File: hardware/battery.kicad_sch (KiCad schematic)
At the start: 40 parts, among them J301 B2B-XH-A, J302 PRPC001DAAN-RC, Q301 DMG2305UX-7, Q302 DMN2005, Q303 DMN2005, U301 BQ29728DSER, U302 MCP73833T-FCI/MF, U303 MAX17048

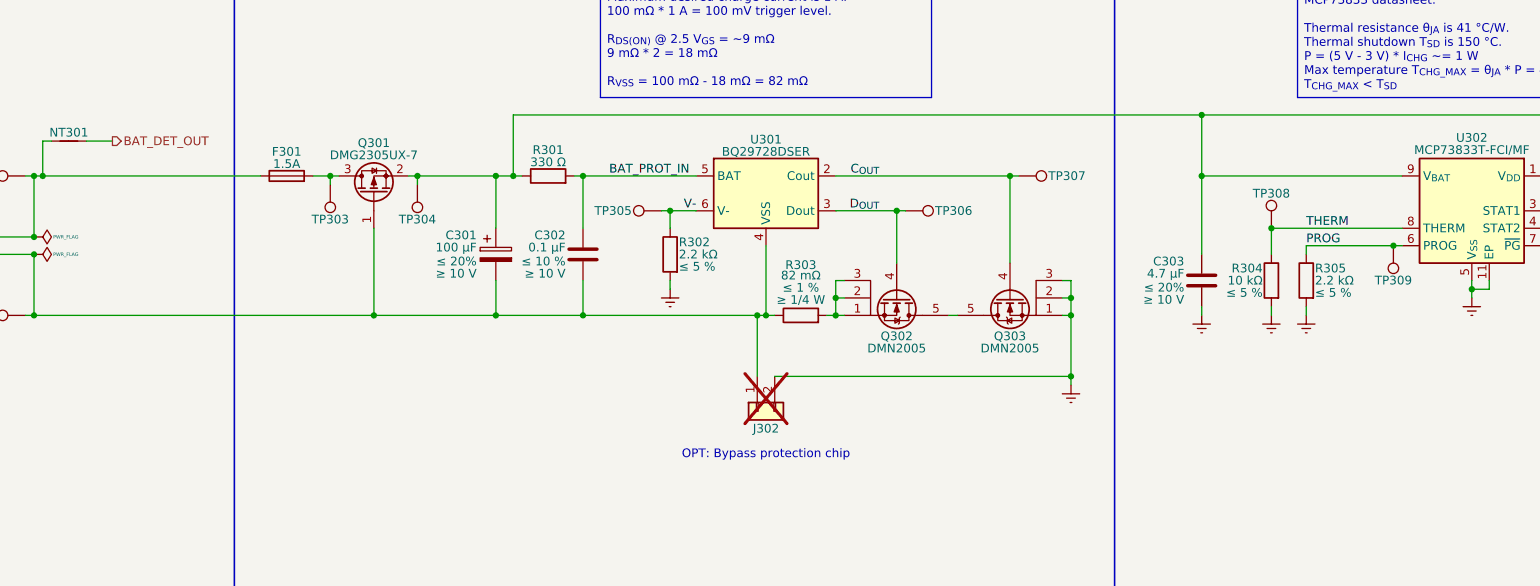
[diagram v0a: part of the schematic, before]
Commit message: HW: Update libraries, fix typos, refine schematics
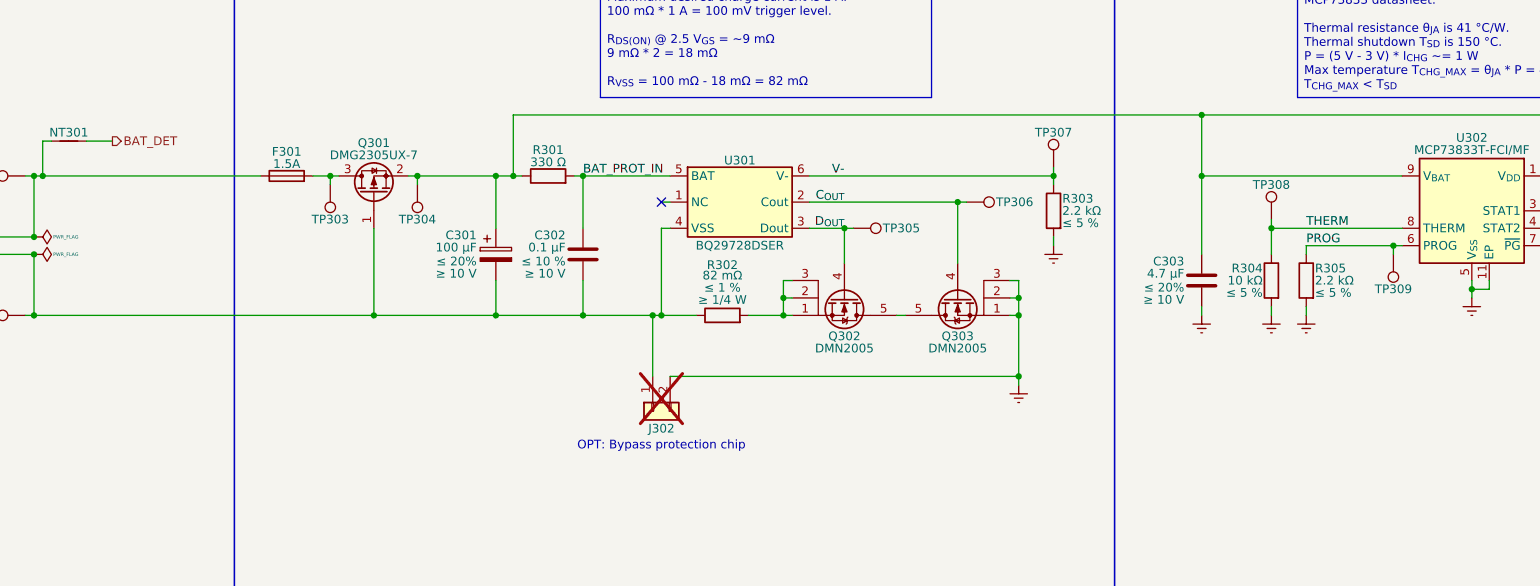
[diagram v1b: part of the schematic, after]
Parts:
- removed TP305: TestPoint, TestPoint:TestPoint_Pad_D1.0mm, symbol Connector:TestPoint
- added TP307: TestPoint, TestPoint:TestPoint_Pad_D1.0mm, symbol Connector:TestPoint
- U301: symbol Battery_Management:BQ297xy -> Texas Instruments:BQ297xy
- renumbered R303 to R302, R302 to R303, TP306 to TP305, TP307 to TP306
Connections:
- net V-: now also TP307.1
- net BAT_DET_OUT renamed BAT_DET
- no-connect marks 0 -> 1
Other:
- moved on the sheet: J302, Q302, Q303, R302, R303, TP305, TP306, TP308, TP309

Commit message: HW: Fix BOM
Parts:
- C302, C305: DigiKey Part Number 490-7998-1-ND -> 732-7532-1-ND; MPN GCM155R71C104KA55J -> 885012205037; Manufacturer Murata Electronics -> Würth Elektronik
- Q301: value DMG2305UX-7 -> IRLML6401TRPBF; DigiKey Part Number DMG2305UX-7DICT-ND -> IRLML6401PBFCT-ND; MPN DMG2305UX-7 -> IRLML6401TRPBF; Manufacturer Diodes Incorporated -> Infineon Technologies
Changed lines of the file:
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@@
 			)
 		)
-		(property "Manufacturer" "Murata Electronics"
+		(property "Manufacturer" "Würth Elektronik"
 			(at 132.08 201.93 0)
 			(effects
@@
 			)
 		)
-		(property "MPN" "GCM155R71C104KA55J"
+		(property "MPN" "885012205037"
 			(at 132.08 201.93 0)
 			(effects
@@
 			)
 		)
-		(property "DigiKey Part Number" "490-7998-1-ND"
+		(property "DigiKey Part Number" "732-7532-1-ND"
 			(at 132.08 201.93 0)
 			(effects
@@
 			)
 		)
-		(property "Manufacturer" "Murata Electronics"
+		(property "Manufacturer" "Würth Elektronik"
 			(at 351.79 186.69 0)
 			(effects
@@
 			)
 		)
-		(property "MPN" "GCM155R71C104KA55J"
+		(property "MPN" "885012205037"
 			(at 351.79 186.69 0)
 			(effects
@@
 			)
 		)
-		(property "DigiKey Part Number" "490-7998-1-ND"
+		(property "DigiKey Part Number" "732-7532-1-ND"
 			(at 351.79 186.69 0)
 			(effects
@@
 			)
 		)
-		(property "Value" "DMG2305UX-7"
+		(property "Value" "IRLML6401TRPBF"
 			(at 101.6 188.214 90)
 			(effects
@@
 			)
 		)
-		(property "Manufacturer" "Diodes Incorporated"
+		(property "Manufacturer" "Infineon Technologies"
 			(at 101.6 193.04 90)
 			(effects
@@
 			)
 		)
-		(property "MPN" "DMG2305UX-7"
+		(property "MPN" "IRLML6401TRPBF"
 			(at 101.6 193.04 90)
 			(effects
@@
 			)
 		)
-		(property "DigiKey Part Number" "DMG2305UX-7DICT-ND"
+		(property "DigiKey Part Number" "IRLML6401PBFCT-ND"
 			(at 101.6 193.04 90)
 			(effects

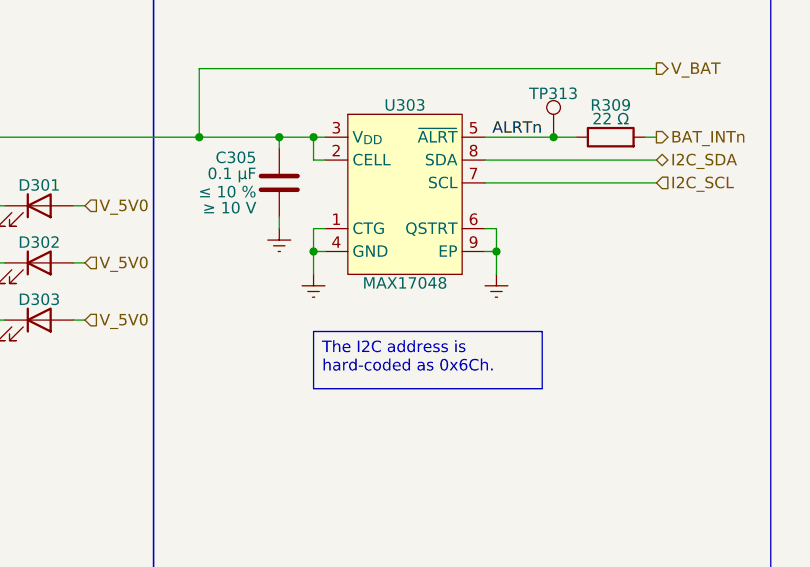
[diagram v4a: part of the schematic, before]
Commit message: HW: Layout USB and Battery
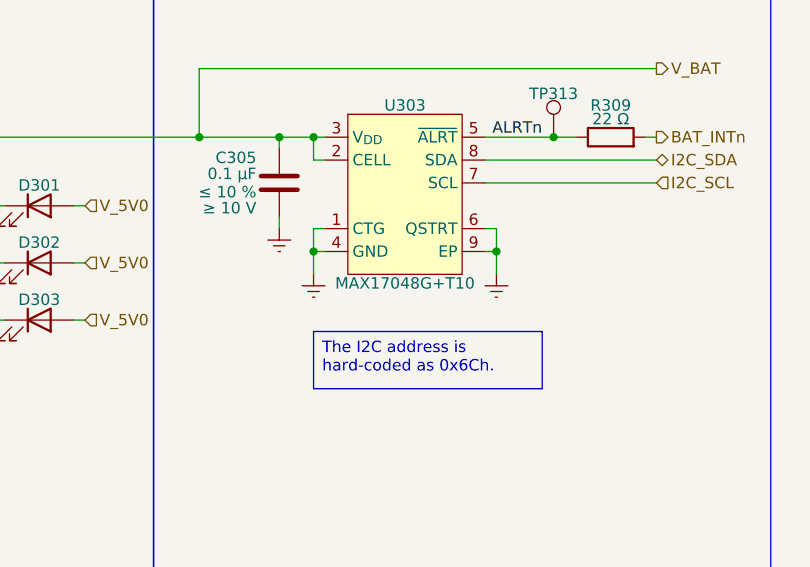
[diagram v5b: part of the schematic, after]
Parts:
- U303: value MAX17048 -> MAX17048G+T10
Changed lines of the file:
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@@
 			)
 		)
-		(property "Value" "MAX17048"
+		(property "Value" "MAX17048G+T10"
 			(at 365.76 197.104 0)
 			(effects

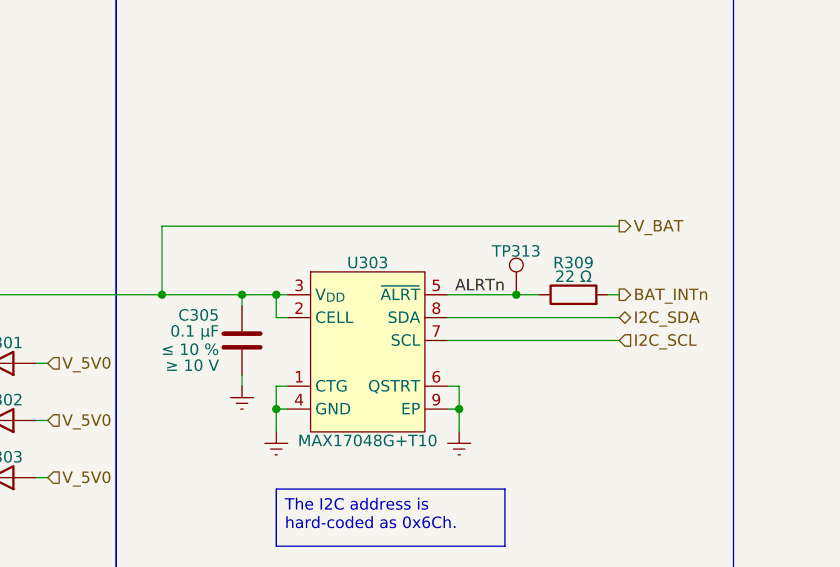
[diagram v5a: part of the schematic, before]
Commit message: HW: Refine power section
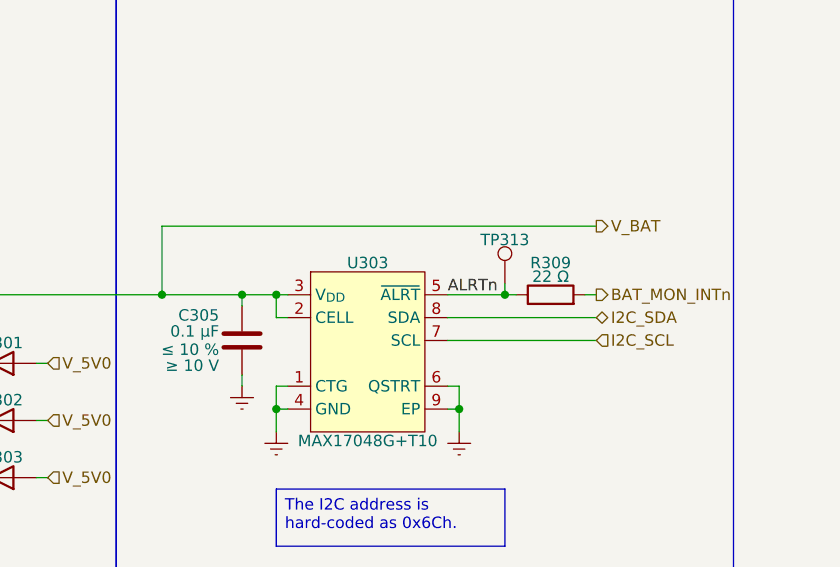
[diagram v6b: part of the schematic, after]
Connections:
- net BAT_INTn renamed BAT_MON_INTn
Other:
- moved on the sheet: R309, TP313
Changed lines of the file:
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@@
 	)
 	(junction
+		(at 381 181.61)
+		(diameter 0)
+		(color 0 0 0 0)
+	)
+	(junction
 		(at 261.62 207.01)
 		(diameter 0)
@@
 	)
 	(junction
-		(at 382.27 181.61)
-		(diameter 0)
-		(color 0 0 0 0)
-	)
-	(junction
 		(at 132.08 190.5)
 		(diameter 0)
@@
 	(wire
 		(pts
+			(xy 381 180.34) (xy 381 181.61)
+		)
+		(stroke
+			(width 0)
+			(type default)
+		)
+	)
+	(wire
+		(pts
 			(xy 237.49 200.66) (xy 250.19 200.66)
 		)
@@
 	(wire
 		(pts
-			(xy 374.65 184.15) (xy 393.7 184.15)
+			(xy 374.65 184.15) (xy 391.16 184.15)
 		)
 		(stroke
@@
 	(wire
 		(pts
-			(xy 382.27 181.61) (xy 384.81 181.61)
+			(xy 195.58 205.74) (xy 195.58 208.28)
 		)
 		(stroke
@@
 	(wire
 		(pts
-			(xy 195.58 205.74) (xy 195.58 208.28)
+			(xy 355.6 184.15) (xy 356.87 184.15)
 		)
 		(stroke
@@
 	(wire
 		(pts
-			(xy 355.6 184.15) (xy 356.87 184.15)
+			(xy 351.79 181.61) (xy 351.79 182.88)
 		)
 		(stroke
@@
 	(wire
 		(pts
-			(xy 351.79 181.61) (xy 351.79 182.88)
+			(xy 382.27 181.61) (xy 381 181.61)
 		)
 		(stroke
@@
 	(wire
 		(pts
-			(xy 374.65 186.69) (xy 393.7 186.69)
+			(xy 374.65 186.69) (xy 391.16 186.69)
 		)
 		(stroke
@@
 	(wire
 		(pts
-			(xy 342.9 173.99) (xy 393.7 173.99)
+			(xy 342.9 173.99) (xy 391.16 173.99)
 		)
 		(stroke
@@
 	(wire
 		(pts
-			(xy 392.43 181.61) (xy 393.7 181.61)
+			(xy 389.89 181.61) (xy 391.16 181.61)
 		)
 		(stroke
@@
 	(wire
 		(pts
-			(xy 374.65 181.61) (xy 382.27 181.61)
+			(xy 374.65 181.61) (xy 381 181.61)
 		)
 		(stroke
@@
 	)
 	(label "ALRTn"
-		(at 381 181.61 180)
+		(at 374.65 181.61 0)
 		(effects
 			(font
 				(size 1.27 1.27)
 			)
-			(justify right bottom)
+			(justify left bottom)
 		)
 	)
@@
 	(hierarchical_label "V_BAT"
 		(shape output)
-		(at 393.7 173.99 0)
+		(at 391.16 173.99 0)
 		(effects
 			(font
@@
 		)
 	)
-	(hierarchical_label "BAT_INTn"
+	(hierarchical_label "BAT_MON_INTn"
 		(shape output)
-		(at 393.7 181.61 0)
+		(at 391.16 181.61 0)
 		(effects
 			(font
@@
 	(hierarchical_label "I2C_SDA"
 		(shape bidirectional)
-		(at 393.7 184.15 0)
+		(at 391.16 184.15 0)
 		(effects
 			(font
@@
 	(hierarchical_label "I2C_SCL"
 		(shape input)
-		(at 393.7 186.69 0)
+		(at 391.16 186.69 0)
 		(effects
 			(font
@@
 	(symbol
 		(lib_id "Device:R")
-		(at 388.62 181.61 90)
+		(at 386.08 181.61 90)
 		(unit 1)
 		(exclude_from_sim no)
@@
 		(dnp no)
 		(property "Reference" "R309"
-			(at 388.62 178.816 90)
+			(at 386.08 178.816 90)
 			(effects
 				(font
@@
 		)
 		(property "Value" "22 Ω"
-			(at 388.62 180.34 90)
+			(at 386.08 180.34 90)
 			(effects
 				(font
@@
 		)
 		(property "Footprint" "perfect_footprints:R_0402_1005Metric"
-			(at 388.62 183.388 90)
+			(at 386.08 183.388 90)
 			(effects
 				(font
@@
 		)
 		(property "Datasheet" "~"
-			(at 388.62 181.61 0)
+			(at 386.08 181.61 0)
 			(effects
 				(font
@@
 		)
 		(property "Description" ""
-			(at 388.62 181.61 0)
+			(at 386.08 181.61 0)
 			(effects
 				(font
@@
 		)
 		(property "Manufacturer" "Würth Elektronik"
-			(at 388.62 181.61 0)
+			(at 386.08 181.61 0)
 			(effects
 				(font
@@
 		)
 		(property "MPN" "560112110046"
-			(at 388.62 181.61 0)
+			(at 386.08 181.61 0)
 			(effects
 				(font
@@
 		)
 		(property "Size" "0402"
-			(at 388.62 181.61 0)
+			(at 386.08 181.61 0)
 			(effects
 				(font
@@
 		)
 		(property "DigiKey Part Number" "732-560112110046CT-ND"
-			(at 388.62 181.61 90)
+			(at 386.08 181.61 90)
 			(effects
 				(font
@@
 		)
 		(property "Footprint review check" "+"
-			(at 388.62 181.61 0)
+			(at 386.08 181.61 0)
 			(effects
 				(font
@@
 	(symbol
 		(lib_id "Connector:TestPoint")
-		(at 382.27 181.61 0)
+		(at 381 180.34 0)
 		(unit 1)
 		(exclude_from_sim no)
@@
 		(dnp no)
 		(property "Reference" "TP313"
-			(at 382.27 176.784 0)
+			(at 381 175.514 0)
 			(effects
 				(font
@@
 		)
 		(property "Value" "TestPoint"
-			(at 384.81 179.5779 0)
+			(at 383.54 178.3079 0)
 			(effects
 				(font
@@
 		)
 		(property "Footprint" "TestPoint:TestPoint_Pad_D1.0mm"
-			(at 387.35 181.61 0)
+			(at 386.08 180.34 0)
 			(effects
 				(font
@@
 		)
 		(property "Datasheet" "~"
-			(at 387.35 181.61 0)
+			(at 386.08 180.34 0)
 			(effects
 				(font
@@
 		)
 		(property "Description" "test point"
-			(at 382.27 181.61 0)
+			(at 381 180.34 0)
 			(effects
 				(font
